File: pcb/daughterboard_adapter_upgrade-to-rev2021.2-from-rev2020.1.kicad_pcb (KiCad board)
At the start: 2 copper layers, 20.2 x 52.2 mm, 4 parts, among them U1 MiniF4, U2 SN74LVC1T45DBV, U3 MiniF4

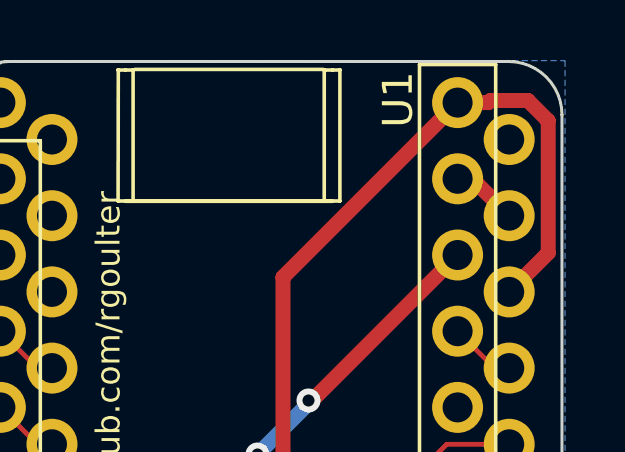
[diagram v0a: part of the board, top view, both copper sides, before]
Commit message: Kicad: Use "5V", "GND", "3V3" in symbol and footprint; update Sch+PCBs
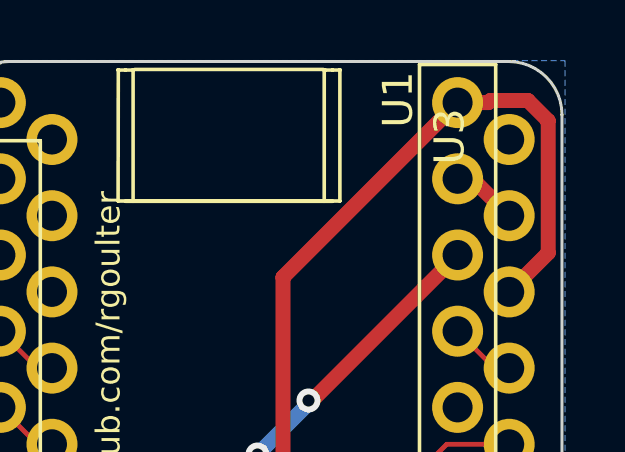
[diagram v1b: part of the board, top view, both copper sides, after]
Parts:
- U1, U3: footprint ProjectLocal:WeAct_MiniF4 -> ProjectLocal:WeAct_MiniF4_Staggerable_rev2020.1
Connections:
- U3 pad 5V: (no net) -> Net-(U3-Pad5V)

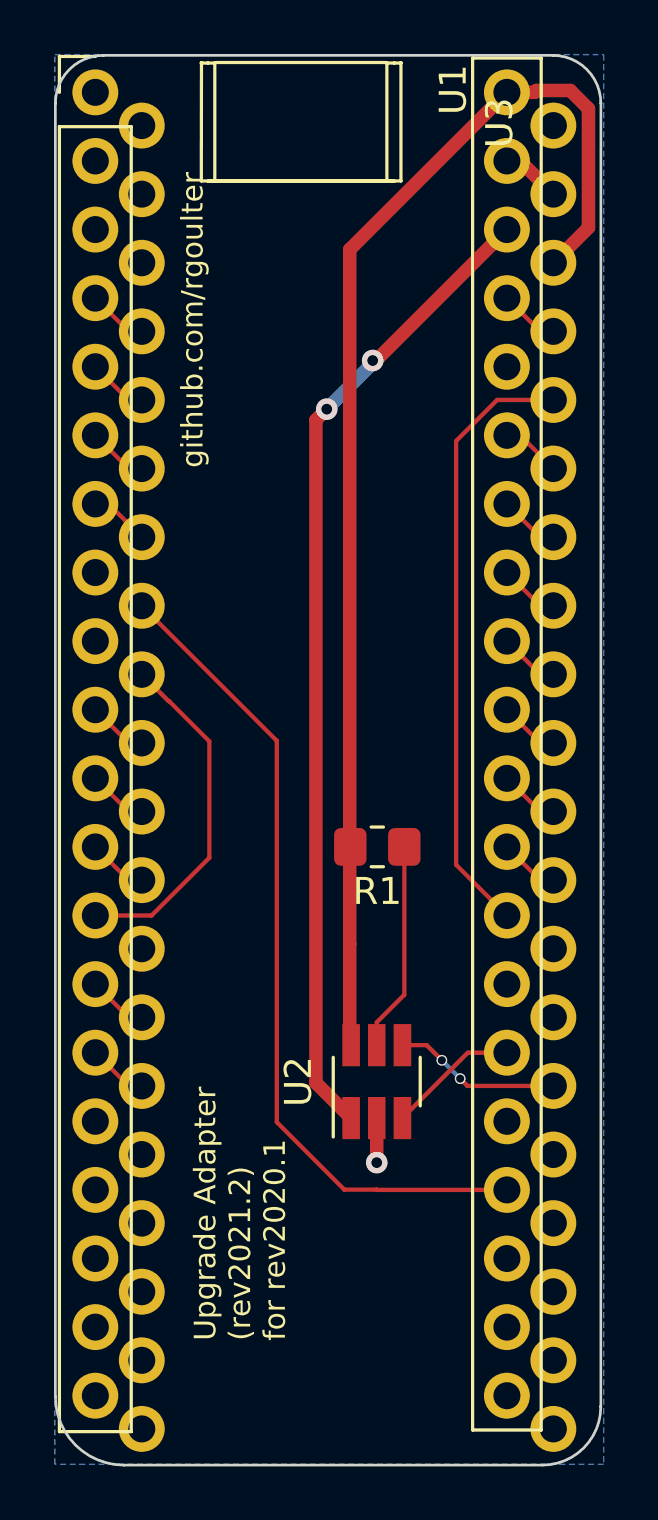
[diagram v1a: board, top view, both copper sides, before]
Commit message: Kicad: plot daughterboards
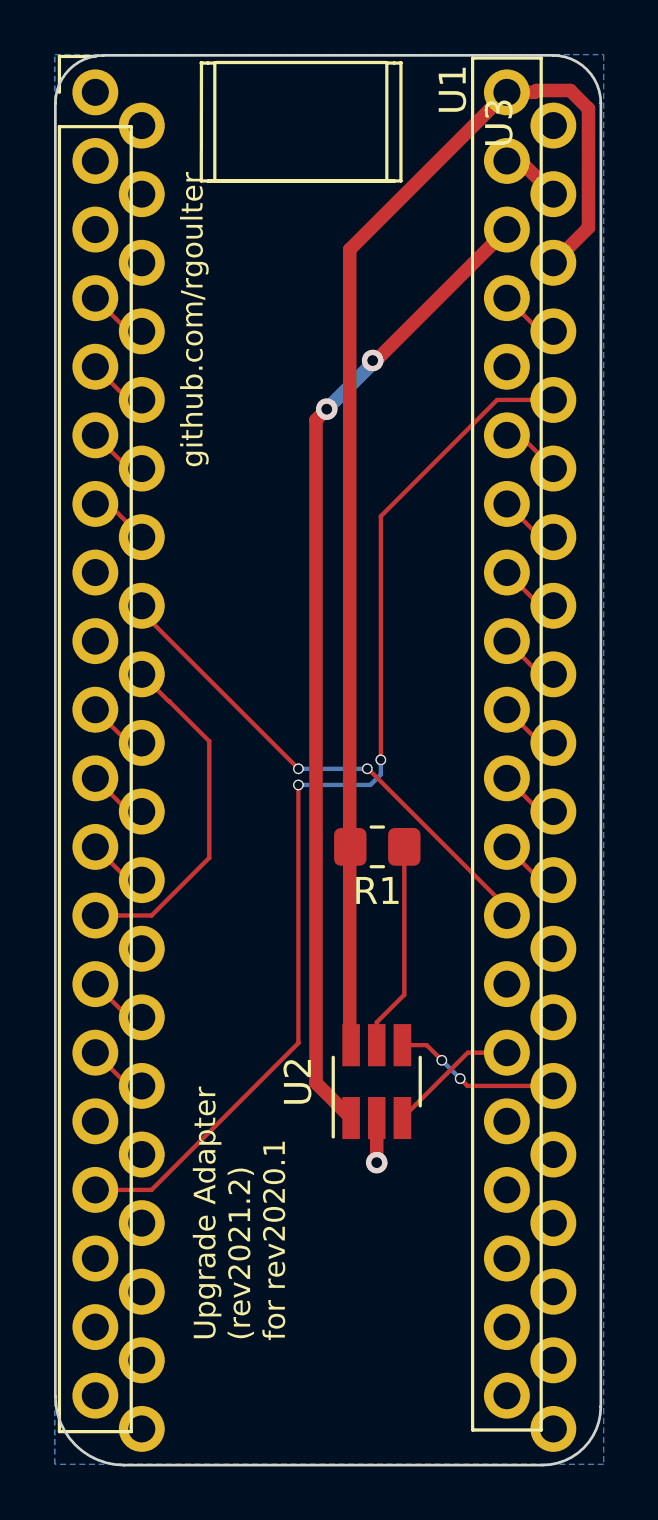
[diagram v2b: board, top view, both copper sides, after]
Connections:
- U1 pad 12: /SW31 -> /SW15
- U1 pad 4: /SW15 -> (no net)
- U1 pad 46: (no net) -> /SW31
- U3 pad 5V: Net-(U3-Pad5V) -> (no net)
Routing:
- net /SW31: track 22.6 -> 40.3 mm, vias 0 -> 2
- net /SW15: track 30.8 -> 18.6 mm, vias 0 -> 2
